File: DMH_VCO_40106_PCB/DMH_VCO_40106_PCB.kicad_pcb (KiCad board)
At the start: 2 copper layers, 98 x 175 mm, 159 parts, among them J1 TS_Jack_6.35mm_Sw, J10 Panel_GND, J100 IDC_02x08, J150 Conn_01x12, J2 TS_Jack_6.35mm_Sw, J200 IDC_02x05, J3 TS_Jack_6.35mm_Sw, J300 AVR-ISP-6, J4 TS_Jack_6.35mm_Sw, J5 TS_Jack_6.35mm_Sw, J6 TS_Jack_6.35mm_Sw, J7 TS_Jack_6.35mm_Sw, J8 TS_Jack_6.35mm_Sw, J9 TS_Jack_6.35mm_Sw, Q1 BC558, Q2 BC548, Q3 BC548, Q4 BC548, Q5 BC548, Q6 BC548, Q7 J113, SW1 SW_SPDT_321_OnOff, SW2 SW_SPDT_321_OnOff, SW3 SW_SPDT_321_OnOff, U1 40106, U2 TL074, U3 TL074, U4 TL074, U5 ATtiny4313-P, U6 SM420561N

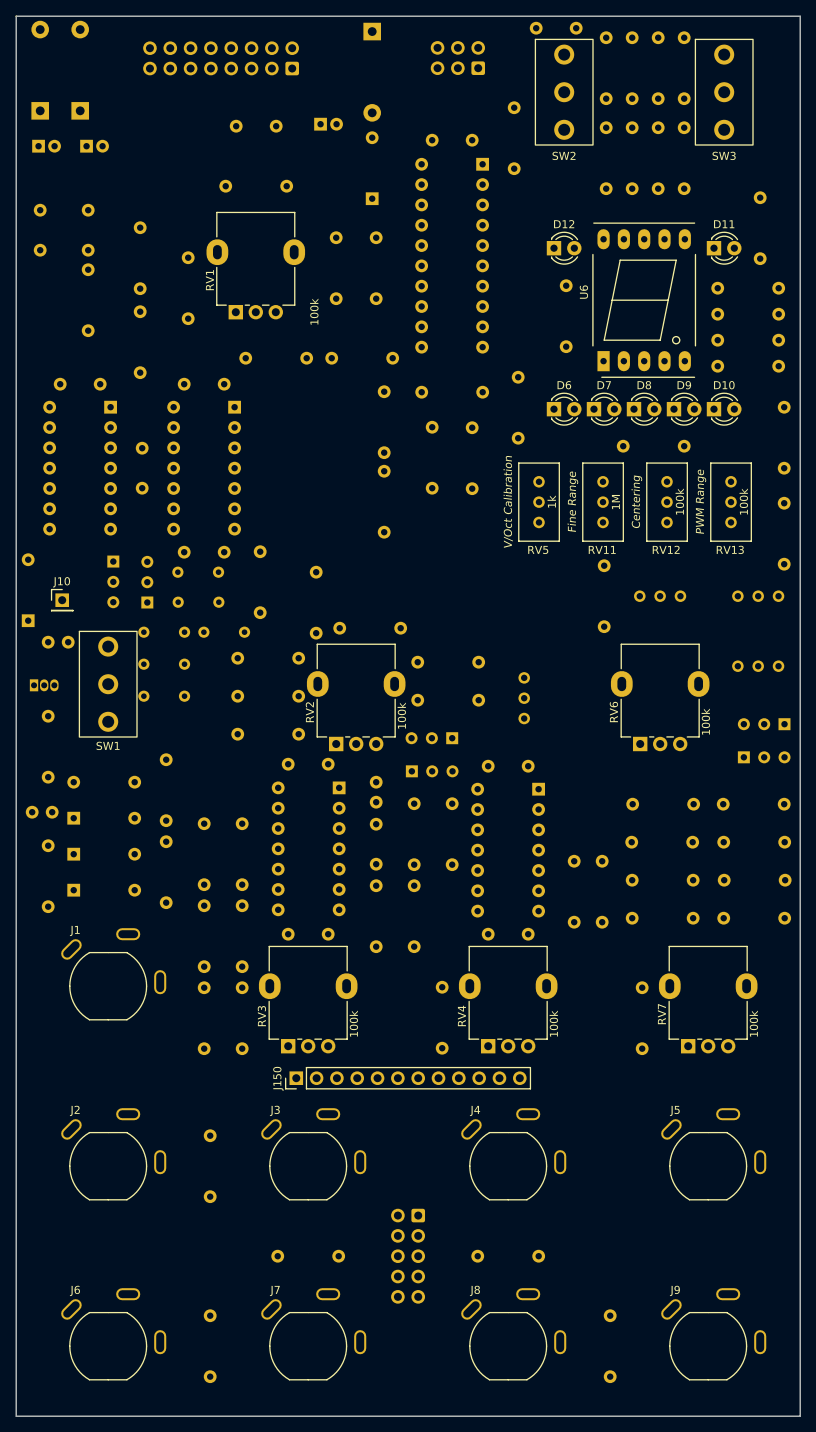
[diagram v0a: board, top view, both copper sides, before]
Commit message: Routed power lines
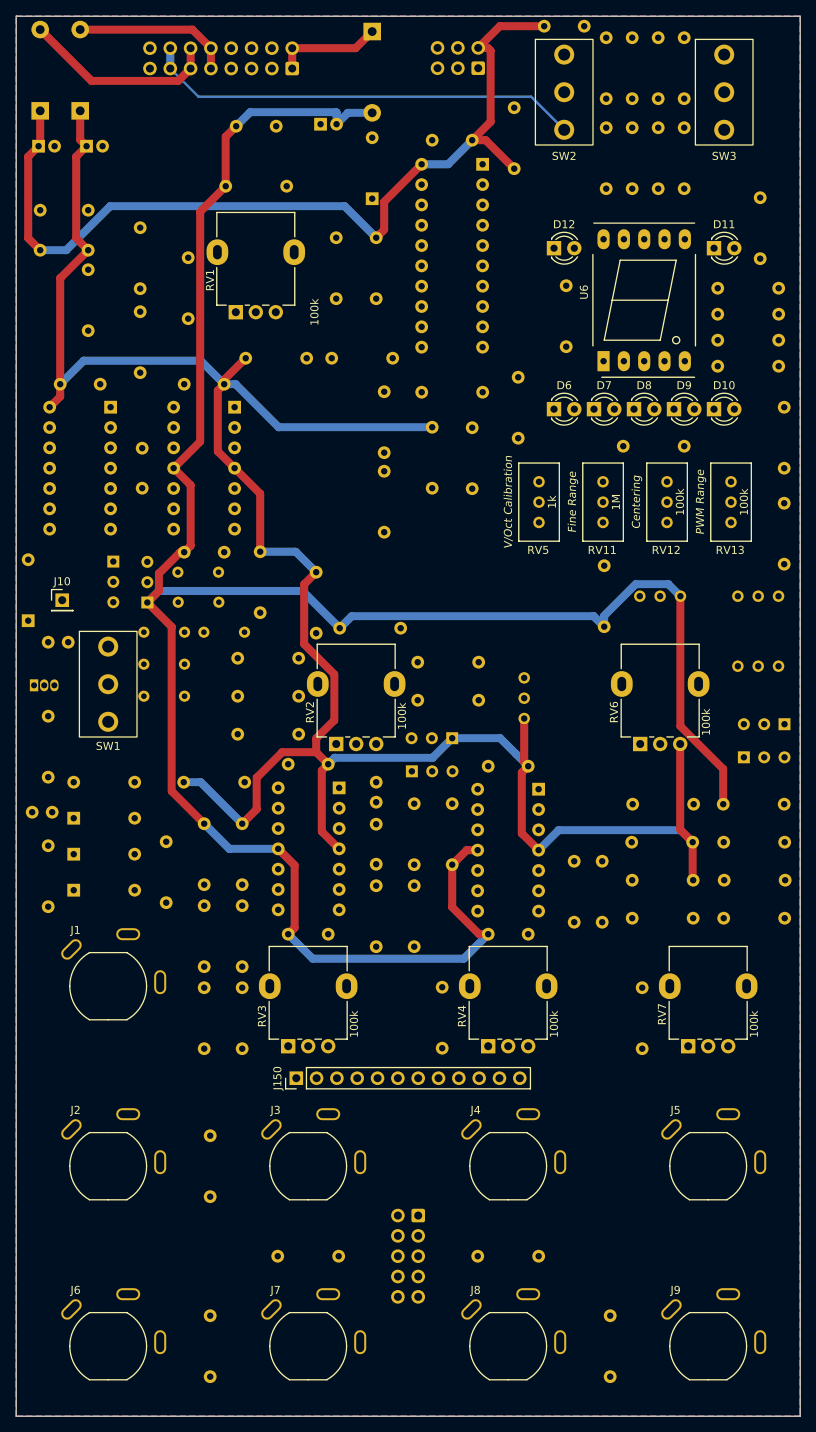
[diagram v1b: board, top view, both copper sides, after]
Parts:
- moved R47 10.9 mm to (79.6, 158.2), turned to 180 degrees
- moved C5 5.00 mm to (56.5, 108.5), turned to 0 degrees
- moved C19 4.01 mm to (117.0, 63.8), turned to 0 degrees
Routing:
- net -12V: track 0.00 -> 283.8 mm
- net +12V: track 0.00 -> 276.1 mm
- net +5V: track 0.00 -> 113.6 mm
- net /Inpus and Outputs/Bus CV: track 0.00 -> 55.0 mm
- net Net-(D15-A): track 0.00 -> 24.6 mm
- net Net-(D14-A): track 0.00 -> 19.8 mm
- net Net-(D13-K): track 0.00 -> 13.4 mm
- added copper zone on B.Cu, net GND
- added copper zone on F.Cu, net GND

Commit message: Routing in progress
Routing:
- net Net-(J150-Pin_10): track 0.00 -> 187.8 mm
- net /Core/Sawtooth: track 0.00 -> 116.2 mm
- net Net-(J300-MOSI): track 0.00 -> 95.9 mm
- net Net-(U4B--): track 0.00 -> 87.7 mm
- net Net-(J300-MISO): track 0.00 -> 83.2 mm
- net /Inpus and Outputs/Sine Out Jack: track 0.00 -> 81.7 mm
- net Net-(R43-Pad2): track 0.00 -> 79.6 mm
- net Net-(RV11-Pad3): track 0.00 -> 78.0 mm
- net Net-(R4-Pad2): track 0.00 -> 75.2 mm
- net /Sine Shaper/Triangle In: track 0.00 -> 73.6 mm
- net Net-(R39-Pad1): track 0.00 -> 71.8 mm
- net Net-(Q5-C): track 0.00 -> 64.9 mm
- net Net-(U5-PB4): track 0.00 -> 62.9 mm
- net Net-(Q6-C): track 0.00 -> 56.3 mm
- net Net-(D5-A): track 0.00 -> 54.6 mm
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
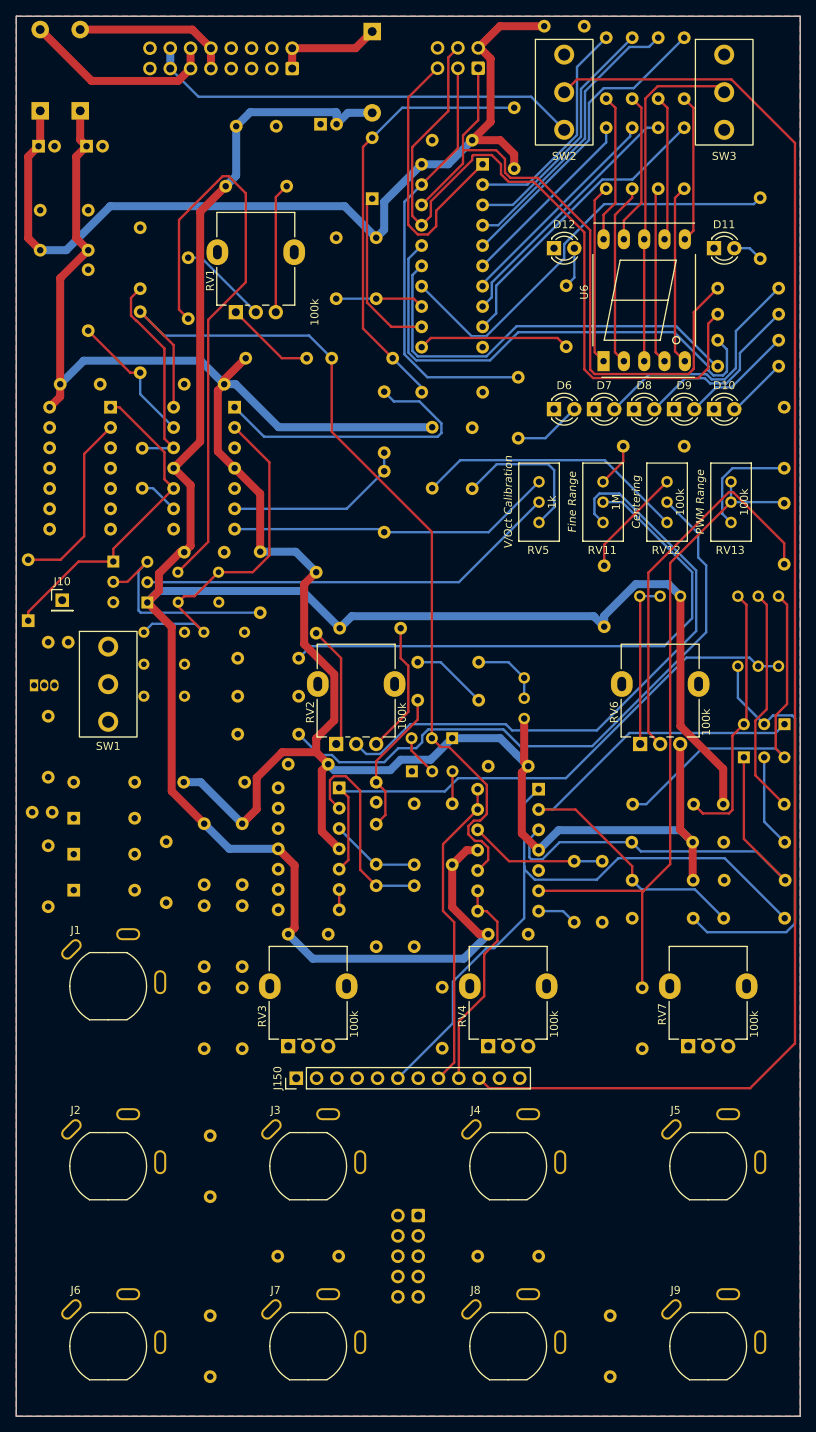
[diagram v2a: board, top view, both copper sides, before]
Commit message: Finished routing main PCB
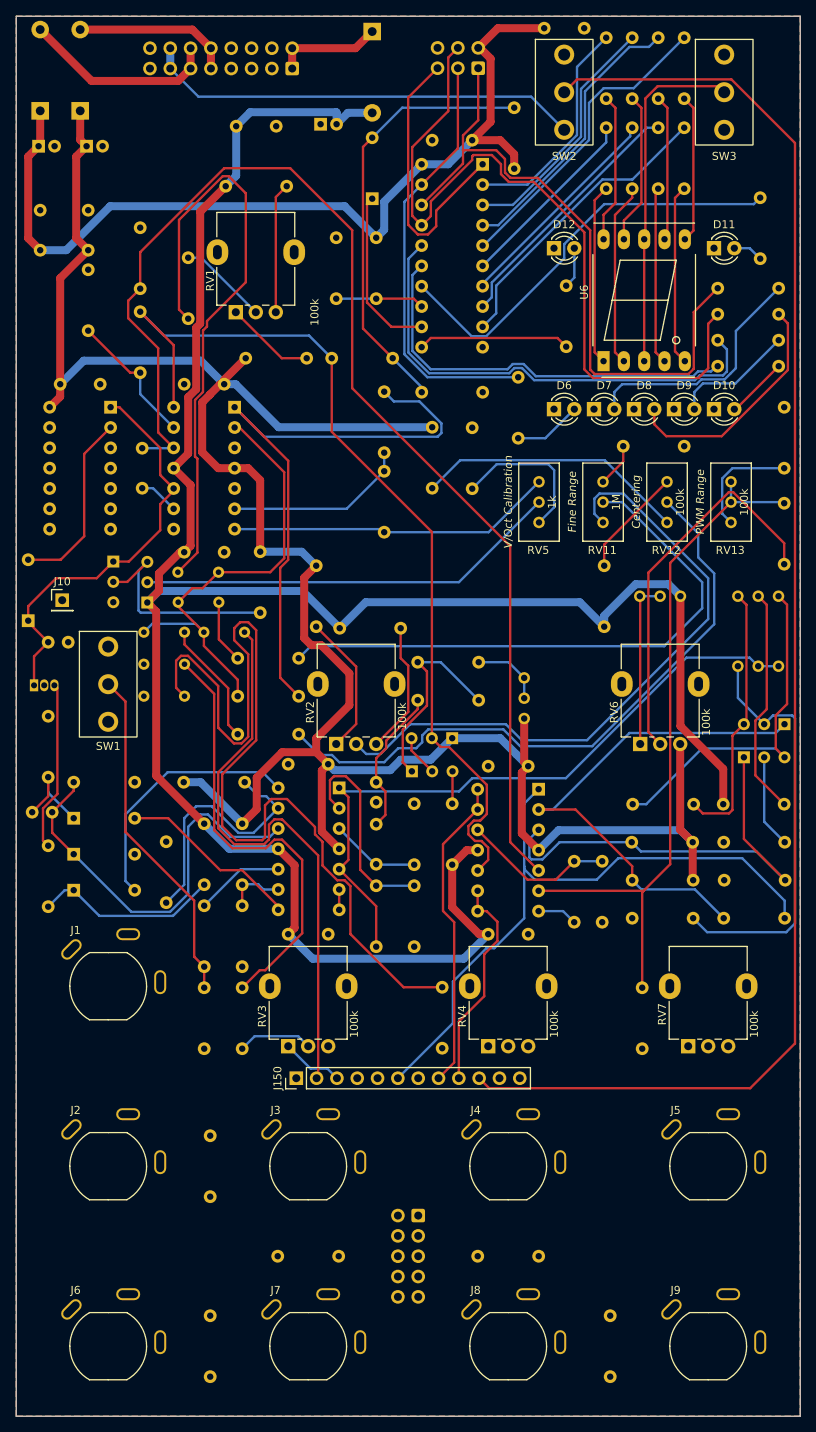
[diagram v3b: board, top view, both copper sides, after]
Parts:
- moved R41 0.81 mm to (88.5, 131.2)
- moved C19 0.25 mm to (117.0, 64.0)
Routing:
- net Net-(U2D-+): track 26.6 -> 155.1 mm
- net Net-(R9-Pad2): track 0.00 -> 114.3 mm
- net /Core/V/Oct In: track 0.00 -> 72.1 mm
- net Net-(R8-Pad2): track 0.00 -> 55.2 mm
- net Net-(D3-K): track 0.00 -> 51.3 mm
- net /Core/Sync In: track 0.00 -> 42.9 mm
- net Net-(R10-Pad2): track 37.6 -> 77.8 mm
- net Net-(U3D--): track 0.00 -> 32.1 mm
- net Net-(D4-A): track 0.00 -> 32.0 mm
- net Net-(D4-K): track 0.00 -> 23.3 mm
- net Net-(D2-A): track 0.00 -> 22.9 mm
- net Net-(Q7-G): track 0.00 -> 21.2 mm
- net Net-(Q4-C): track 9.59 -> 25.4 mm
- net Net-(R43-Pad1): track 0.00 -> 15.5 mm
- net Net-(U2A--): track 45.1 -> 58.0 mm
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
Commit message: Limited main PCB and finished routing
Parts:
- removed J1, J2, J3, J4, J5, J6, J7, J8, J9: TS_Jack_6.35mm_Sw, SynthStuff:CUI_MJ-63052A
- removed J200: IDC_02x05, SynthStuff:IDC-Header_2x05_P2.54mm_Vertical_BackBone
- removed R20, R21, R28, R44: 1k, Resistor_THT:R_Axial_DIN0207_L6.3mm_D2.5mm_P7.62mm_Horizontal
- removed R7: 100k, Resistor_THT:R_Axial_DIN0207_L6.3mm_D2.5mm_P7.62mm_Horizontal
- moved R46 1.50 mm to (69.8, 164.2)
- moved R53 1.50 mm to (55.0, 164.7)
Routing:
- net Net-(J150-Pin_1): track 0.57 -> 71.3 mm
- net /Core/PW Mod In: track 0.00 -> 41.5 mm
- net /Inpus and Outputs/Triangle Out Jack: track 2.54 -> 27.7 mm
- net /Core/Exp FM In 2: track 0.00 -> 20.3 mm
- net Net-(R14-Pad2): track 0.00 -> 9.41 mm
- net Net-(R9-Pad1): track 0.00 -> 9.39 mm
- net Net-(U2A--): track 58.0 -> 66.0 mm
- net /Inpus and Outputs/Sine Out Jack: track 83.0 -> 86.0 mm
- net Net-(U2C--): track 5.00 -> 7.54 mm
- net /Sine Shaper/Triangle In: track 85.2 -> 87.4 mm
- net Net-(D4-K): track 23.3 -> 21.7 mm
- net Net-(U5-PA0/XTAL1): track 38.7 -> 40.2 mm
- net Net-(Q7-G): track 21.2 -> 19.7 mm
- net Net-(U3D--): track 32.1 -> 30.6 mm
- net Net-(U5-PA1/XTAL2): track 35.1 -> 36.5 mm
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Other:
- board size 98 x 175 mm -> 98 x 135 mm

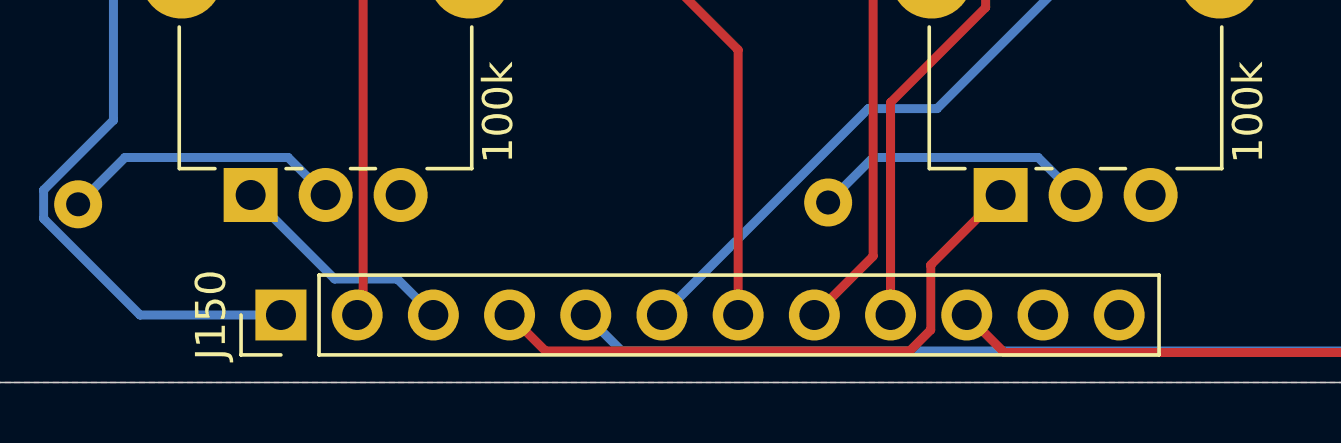
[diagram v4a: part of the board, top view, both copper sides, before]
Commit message: Created separate connectors PCB
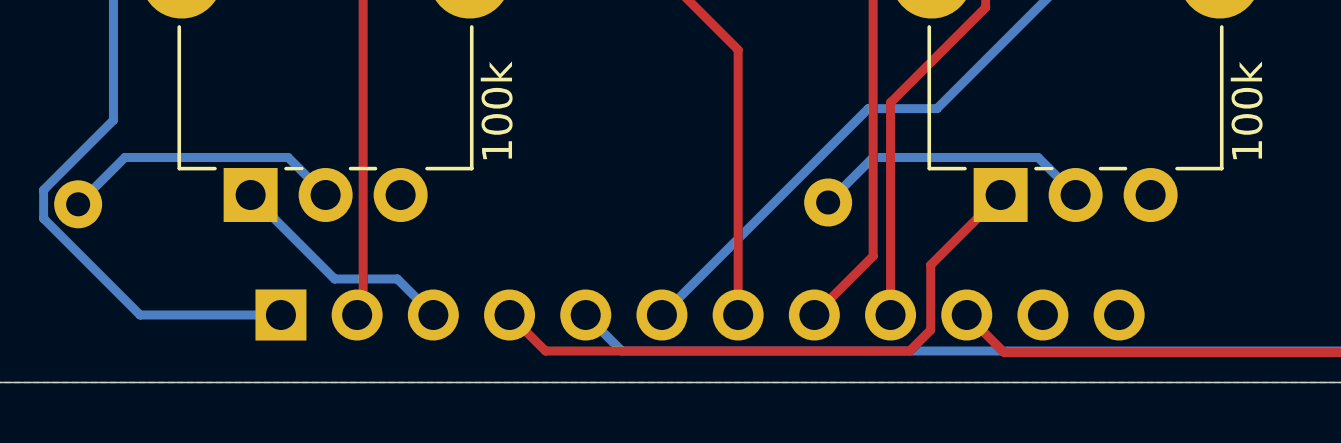
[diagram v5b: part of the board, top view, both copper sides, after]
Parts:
- J150: footprint Connector_PinHeader_2.54mm:PinHeader_1x12_P2.54mm_Vertical -> Connector_PinSocket_2.54mm:PinSocket_1x12_P2.54mm_Vertical; moved to B.Cu
- turned J150 to -90 degrees

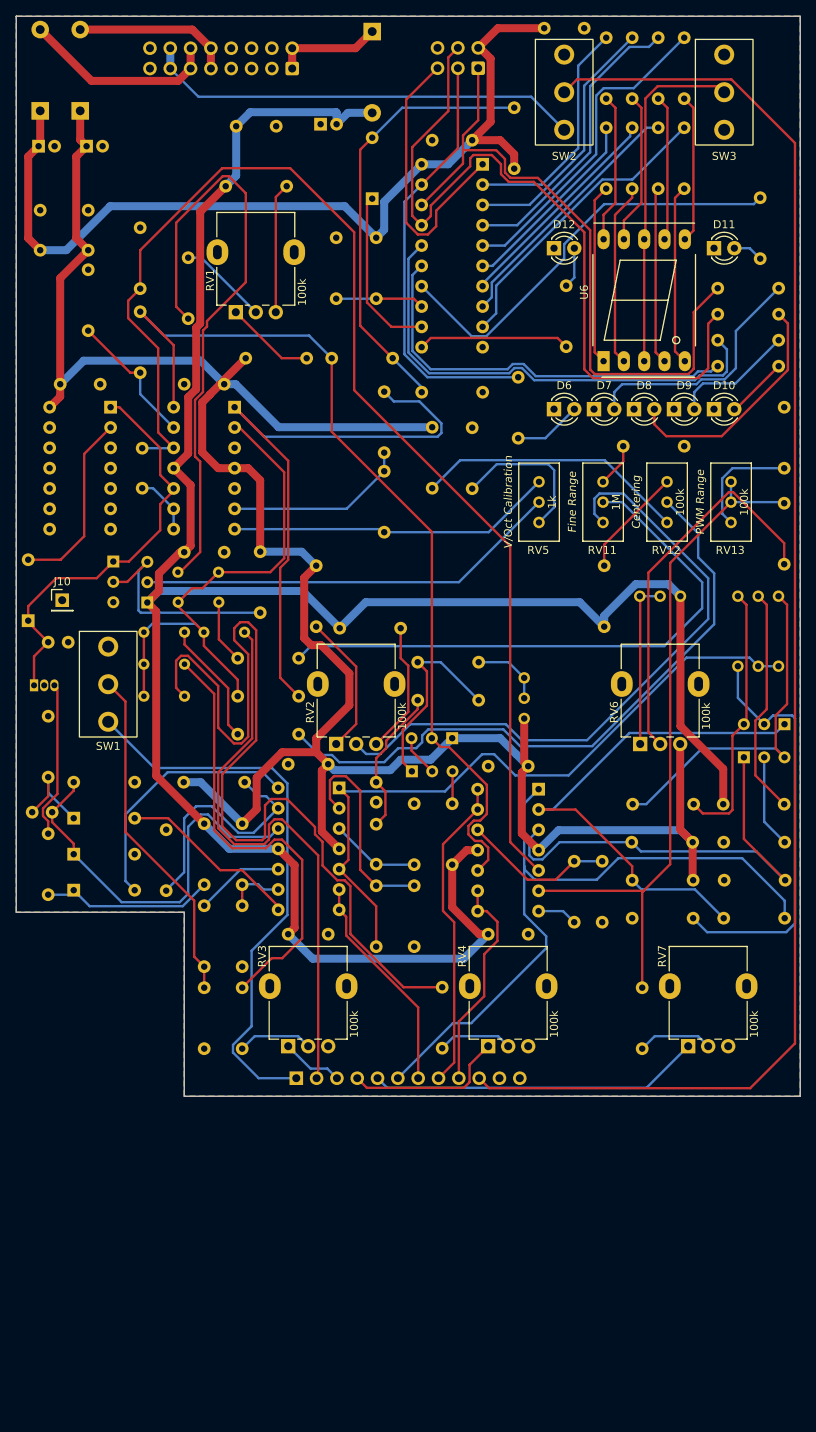
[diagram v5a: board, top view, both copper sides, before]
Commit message: Corrected RD90 pots pin 1 and 3 connections
Otherwise all 6 pots would behave as if inverted
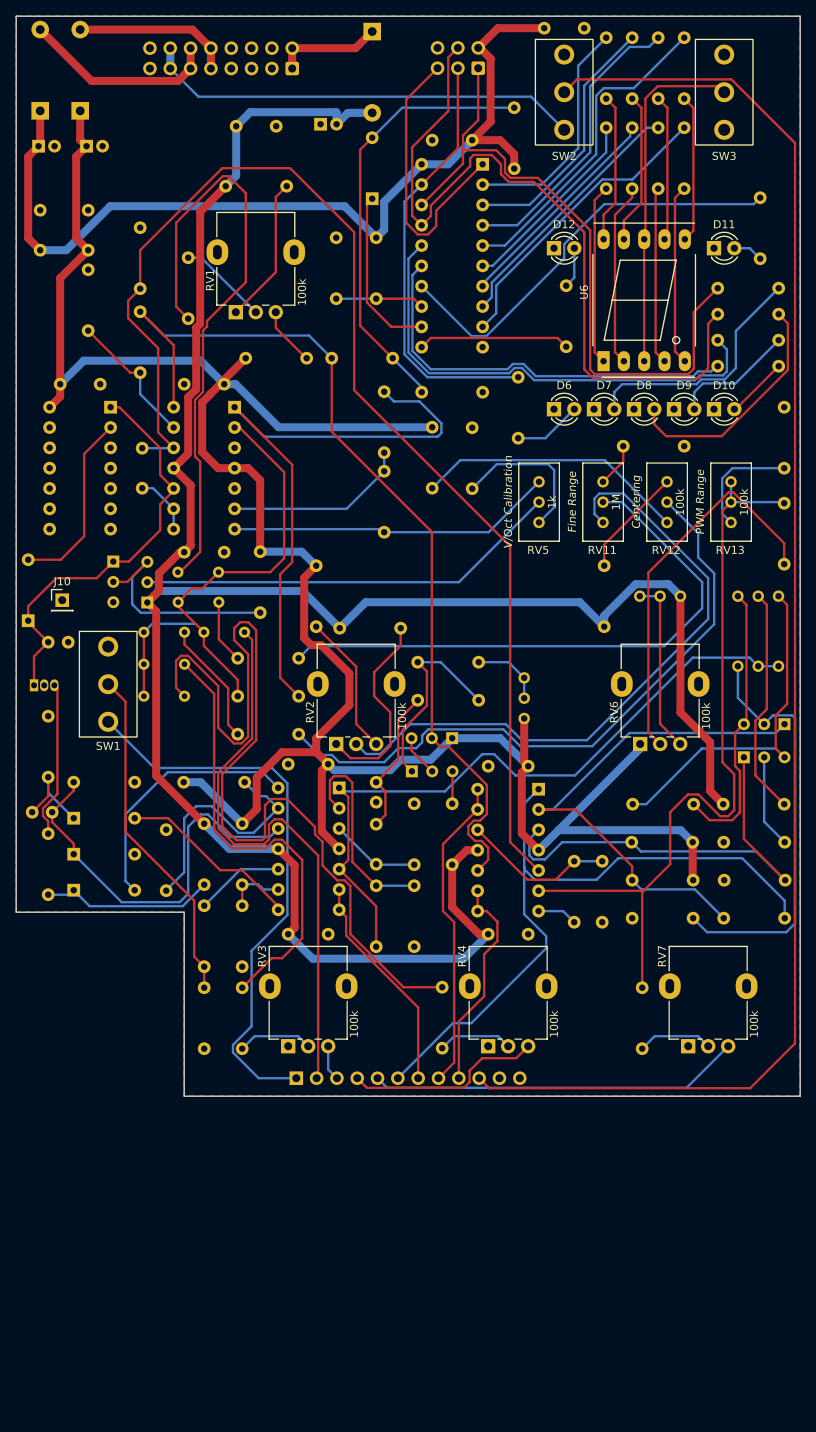
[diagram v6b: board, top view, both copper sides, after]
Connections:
- RV1 pad 1: Net-(R1-Pad1) -> Net-(R2-Pad2)
- RV1 pad 3: Net-(R2-Pad2) -> Net-(R1-Pad1)
- RV2 pad 1: Net-(R41-Pad2) -> Net-(R40-Pad1)
- RV2 pad 3: Net-(R40-Pad1) -> Net-(R41-Pad2)
- RV3 pad 1: /Core/Exp FM In 1 -> GND
- RV3 pad 3: GND -> /Core/Exp FM In 1
- RV4 pad 1: /Core/Exp FM In 2 -> GND
- RV4 pad 3: GND -> /Core/Exp FM In 2
- RV6 pad 1: Net-(RV14-Pad1) -> +12V
- RV6 pad 3: +12V -> Net-(RV14-Pad1)
- RV7 pad 1: /Core/PW Mod In -> GND
- RV7 pad 3: GND -> /Core/PW Mod In
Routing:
- net Net-(R40-Pad1): track 16.5 -> 25.1 mm
- net Net-(U4B--): track 87.7 -> 95.7 mm
- net /Core/PW Mod In: track 41.5 -> 46.5 mm
- net /Core/Exp FM In 2: track 20.3 -> 24.9 mm
- net Net-(R1-Pad1): track 11.2 -> 7.38 mm
- net /Core/Exp FM In 1: track 7.75 -> 4.45 mm
- net +12V: track 283.6 -> 285.7 mm
- net Net-(R2-Pad2): track 16.3 -> 18.4 mm
- net Net-(Q5-E): track 33.4 -> 35.3 mm
- net Net-(RV14-Pad1): track 21.0 -> 22.1 mm
- net Net-(Q1-E): track 27.1 -> 27.8 mm
